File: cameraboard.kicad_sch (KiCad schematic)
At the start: 6 parts, among them J1 Conn_02x05_Odd_Even, Q1 Nikla_Vision, Q2 SSM3J133TU,LF

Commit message: Moved nicla model to kicad_libs, exported pcb model
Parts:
- R1, R2: footprint Resistor_SMD:R_0603_1608Metric_Pad0.98x0.95mm_HandSolder -> (none)
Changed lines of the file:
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@@
       (effects (font (size 0.762 0.762)) (justify left))
     )
-    (property "Footprint" "Resistor_SMD:R_0603_1608Metric_Pad0.98x0.95mm_HandSolder" (id 2) (at 42.672 42.418 0)
+    (property "Footprint" "" (id 2) (at 42.672 42.418 0)
       (effects (font (size 1.27 1.27)) hide)
     )
@@
       (effects (font (size 0.762 0.762)))
     )
-    (property "Footprint" "Resistor_SMD:R_0603_1608Metric_Pad0.98x0.95mm_HandSolder" (id 2) (at 47.625 37.084 0)
+    (property "Footprint" "" (id 2) (at 47.625 37.084 0)
       (effects (font (size 1.27 1.27)) hide)
     )

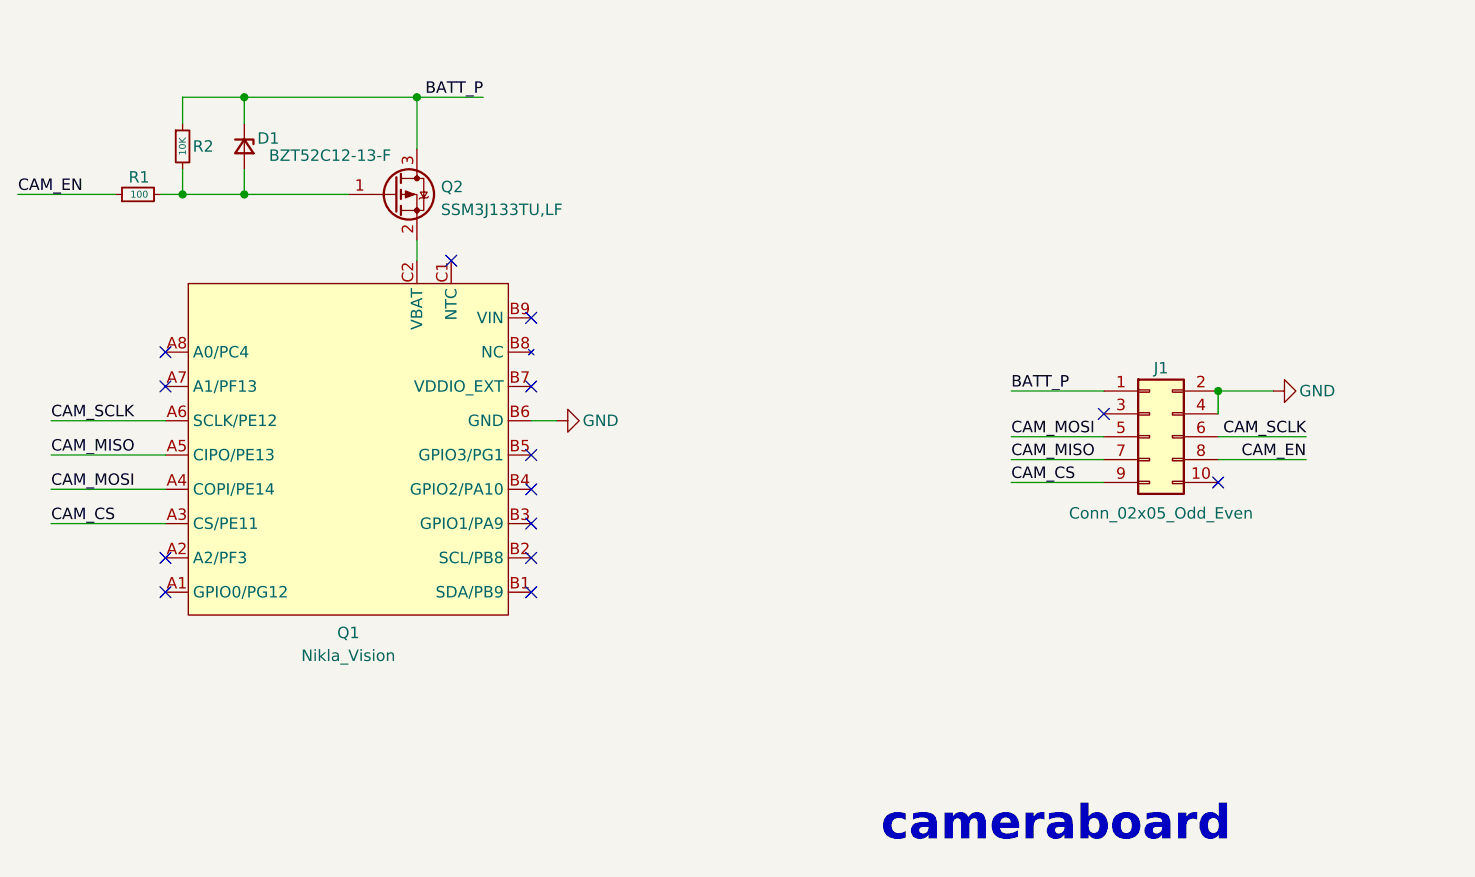
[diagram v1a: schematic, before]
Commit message: Changed board shape and rewired
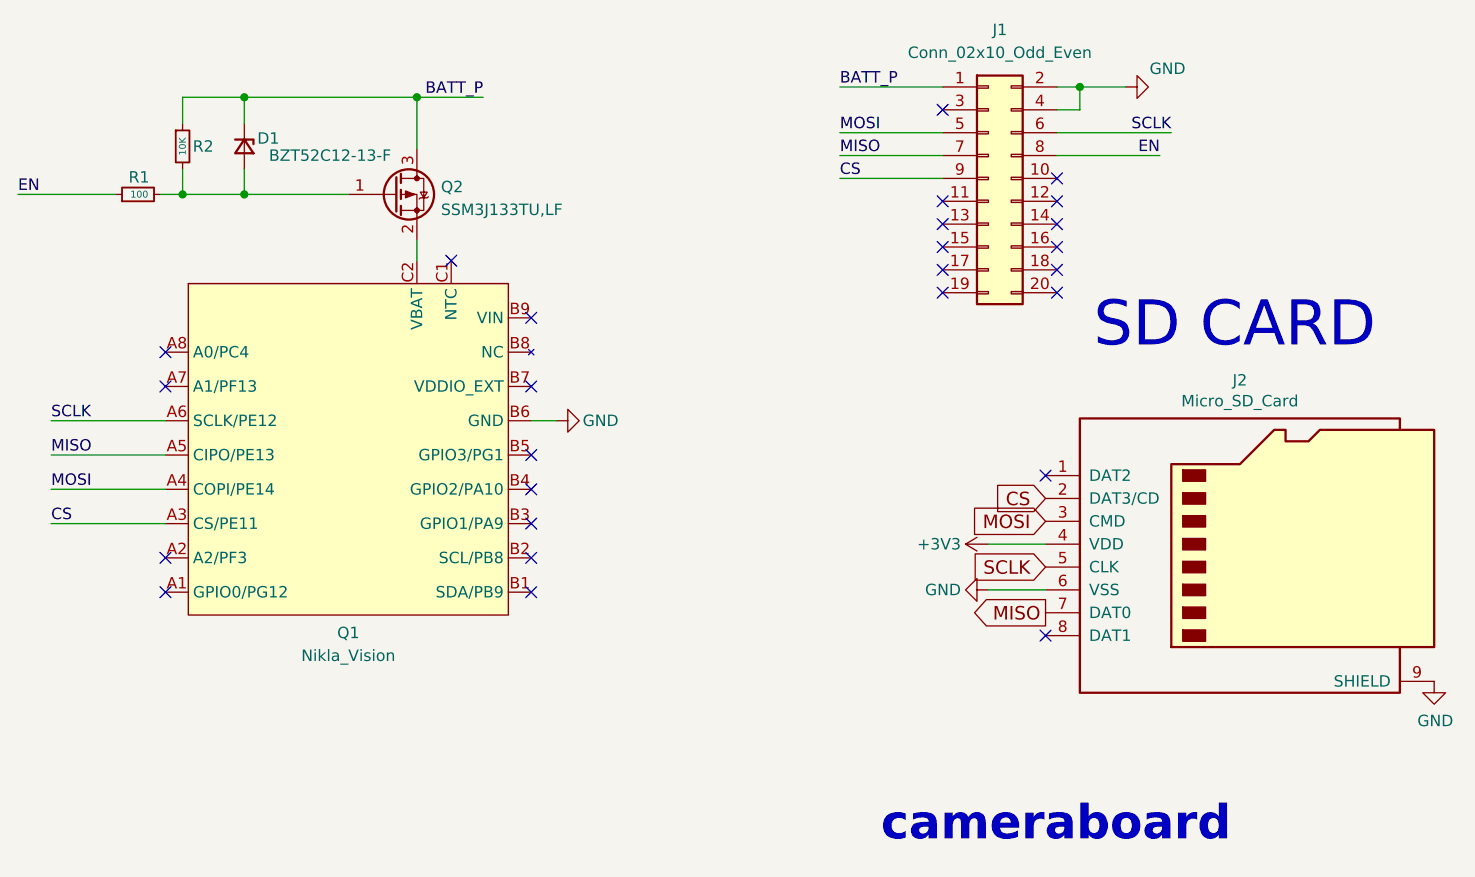
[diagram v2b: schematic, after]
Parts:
- removed J1: Conn_02x05_Odd_Even, Connector_PinSocket_1.27mm:PinSocket_2x05_P1.27mm_Vertical_SMD, symbol Connector_Generic:Conn_02x05_Odd_Even
- added J1: Conn_02x10_Odd_Even, Connector_PinHeader_1.27mm:PinHeader_2x10_P1.27mm_Vertical, symbol Connector_Generic:Conn_02x10_Odd_Even
- added J2: Micro_SD_Card, cameraboard:microSD_HC_Molex_104031-0811, symbol Connector:Micro_SD_Card
- R1, R2: footprint (none) -> Resistor_SMD:R_0603_1608Metric_Pad0.98x0.95mm_HandSolder
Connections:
- net BATT_P: now also J1.1 (Pin_1)
- net GND: now also J1.2 (Pin_2), J1.4 (Pin_4), J2.6 (VSS), J2.9 (SHIELD)
- net CAM_CS renamed CS
- net CS: now also J1.9 (Pin_9), J2.2 (DAT3/CD)
- net CAM_EN renamed EN
- net EN: now also J1.8 (Pin_8)
- net CAM_MISO renamed MISO
- net MISO: now also J1.7 (Pin_7), J2.7 (DAT0)
- net CAM_MOSI renamed MOSI
- net MOSI: now also J1.5 (Pin_5), J2.3 (CMD)
- net CAM_SCLK renamed SCLK
- net SCLK: now also J1.6 (Pin_6), J2.5 (CLK)
- new net +3V3: J2.4 (VDD)
- no-connect marks 14 -> 26
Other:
- note added: "SD CARD"

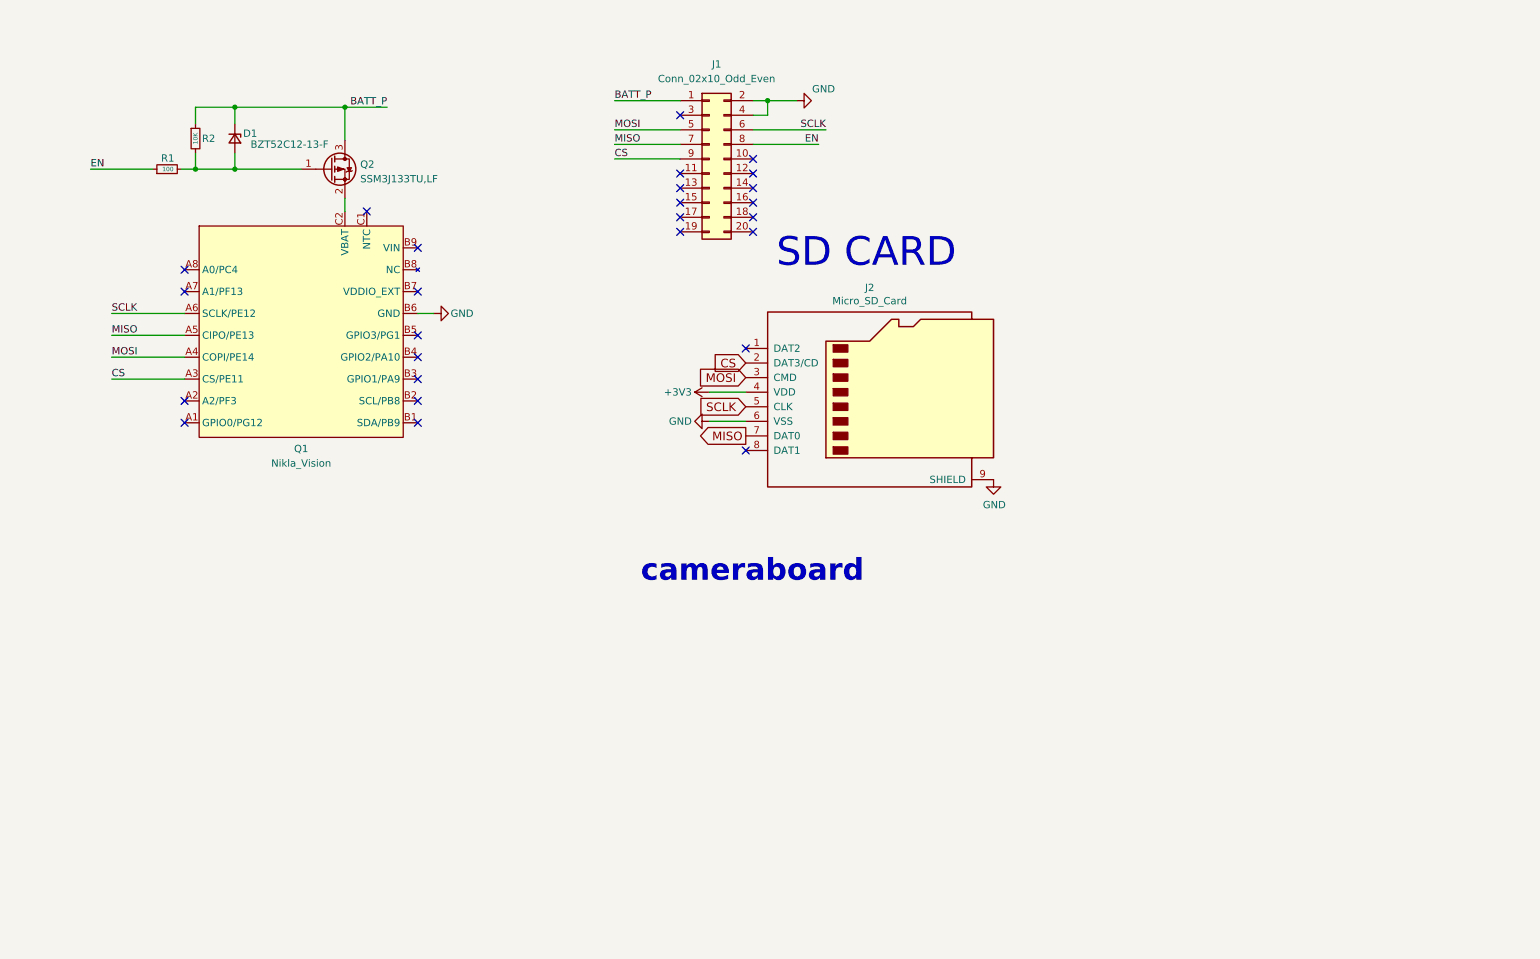
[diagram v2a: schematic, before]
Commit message: Schematic fixes and re-routing
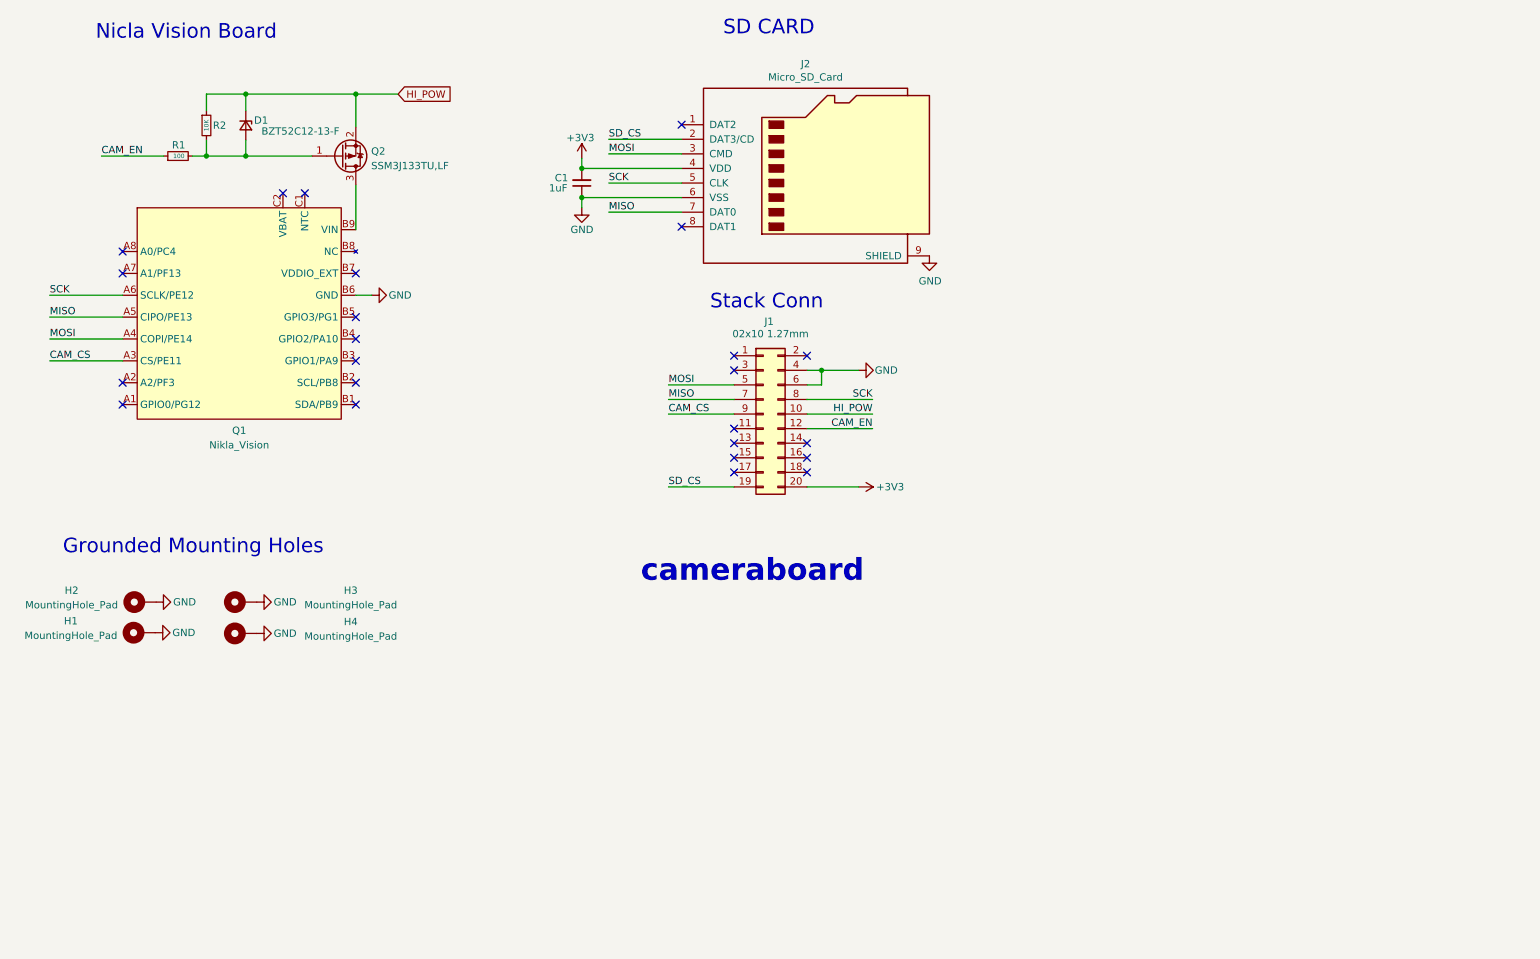
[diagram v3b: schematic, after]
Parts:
- added C1: 1uF, Capacitor_SMD:C_0603_1608Metric_Pad1.08x0.95mm_HandSolder, symbol Device:C_Small
- added H1, H2, H3, H4: MountingHole_Pad, mainboard:MountingHole, symbol Mechanical:MountingHole_Pad
- J1: value Conn_02x10_Odd_Even -> 02x10 1.27mm
- J2: footprint cameraboard:microSD_HC_Molex_104031-0811 -> cameraboard:MOLEX_503398-1892
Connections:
- net +3V3: now also J1.20 (Pin_20), C1.2
- net GND: now also J1.6 (Pin_6), C1.1, H1.1, H2.1, H3.1, H4.1; no longer J1.2 (Pin_2)
- net HI_POW: now reaches J1.10 (Pin_10)
- net HI_POW: now also D1.1 (K), Q2.2 (S), R2.1
- net CAM_EN: now reaches J1.12 (Pin_12)
- net CAM_EN: now also R1.1
- net SD_CS: now reaches J1.19 (Pin_19)
- net SD_CS: now also J2.2 (DAT3/CD)
- net at Q1.B9 (VIN): now also Q2.3 (D)
- net at Q1.C2 (VBAT): no longer Q2.2 (S)
- removed net BATT_P: D1.1 (K), J1.1 (Pin_1), Q2.3 (D), R2.1
- net CS renamed CAM_CS
- net CAM_CS: no longer J2.2 (DAT3/CD)
- net EN renamed SCK
- net SCK: now also J2.5 (CLK), Q1.A6 (SCLK/PE12); no longer R1.1
- removed net SCLK: J1.6 (Pin_6), J2.5 (CLK), Q1.A6 (SCLK/PE12)
- no-connect marks 26 -> 24
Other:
- note added: "Grounded Mounting Holes"
- note added: "Nicla Vision Board"
- note added: "Stack Conn"
- moved on the sheet: D1, J1, J2, Q1, Q2, R1, R2

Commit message: Moved stuff into place
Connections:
- net CAM_EN: now also J1.10 (Pin_10); no longer J1.12 (Pin_12)
- net HI_POW: now also J1.8 (Pin_8); no longer J1.10 (Pin_10)
- net SCK: now also J1.12 (Pin_12); no longer J1.8 (Pin_8)
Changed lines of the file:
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@@
     (effects (font (size 1.27 1.27)) (justify left bottom))
   )
-  (label "CAM_EN" (at 165.608 87.63 180)
+  (label "CAM_EN" (at 165.608 85.09 180)
     (effects (font (size 1.27 1.27)) (justify right bottom))
   )
@@
     (effects (font (size 1.27 1.27)) (justify left bottom))
   )
-  (label "HI_POW" (at 165.608 85.09 180)
+  (label "HI_POW" (at 165.608 82.55 180)
     (effects (font (size 1.27 1.27)) (justify right bottom))
   )
@@
     (effects (font (size 1.27 1.27)) (justify left bottom))
   )
-  (label "SCK" (at 165.608 82.55 180)
+  (label "SCK" (at 165.608 87.63 180)
     (effects (font (size 1.27 1.27)) (justify right bottom))
   )

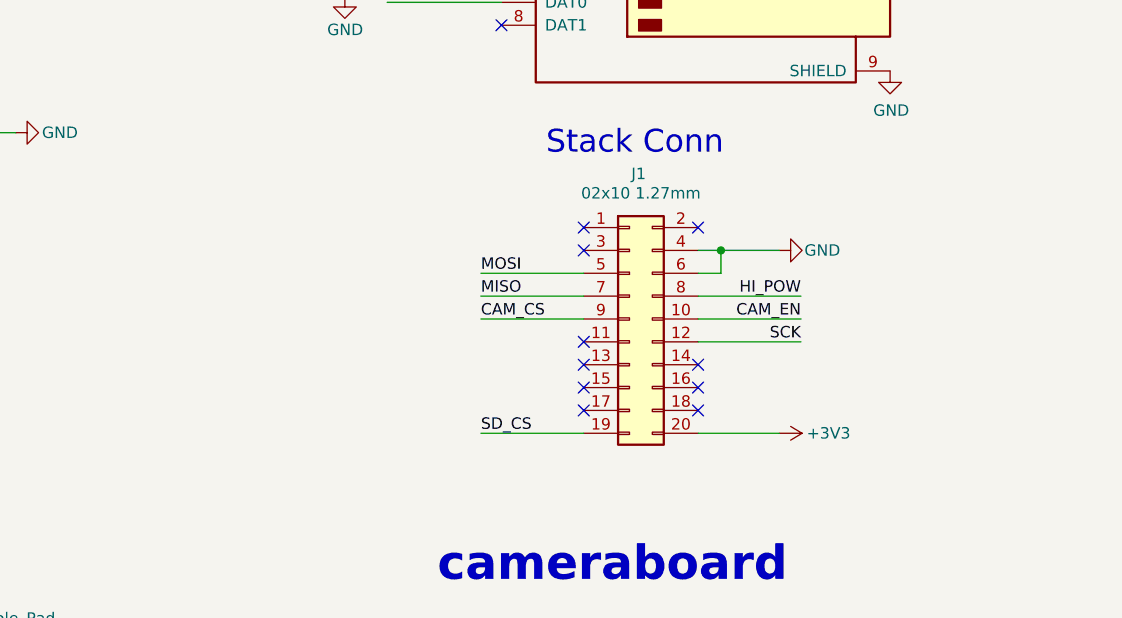
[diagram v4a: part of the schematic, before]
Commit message: stack connectors changes
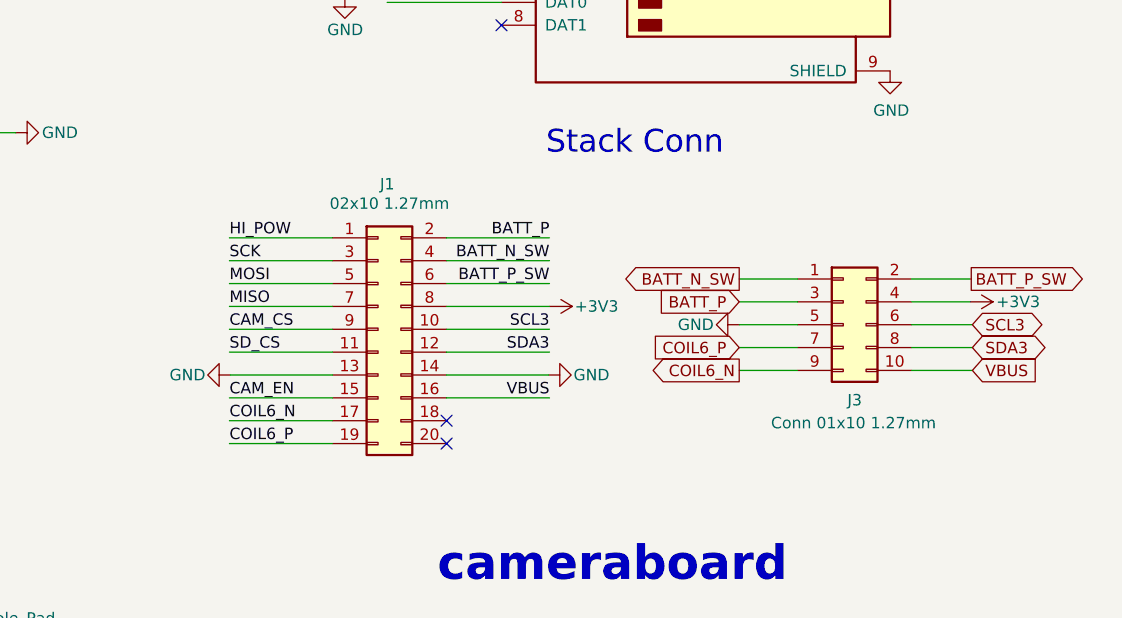
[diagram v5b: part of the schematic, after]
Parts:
- added J3: Conn 01x10 1.27mm, cameraboard:SAMTEC_FLE-105-01-G-DV-A, symbol Connector_Generic:Conn_02x05_Odd_Even
- J1: footprint Connector_PinHeader_1.27mm:PinHeader_2x10_P1.27mm_Vertical -> cameraboard:SAMTEC_TFM-110-12-L-D-A
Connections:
- net +3V3: now also J1.8 (Pin_8), J3.4 (Pin_4); no longer J1.20 (Pin_20)
- net CAM_EN: now also J1.15 (Pin_15); no longer J1.10 (Pin_10)
- net GND: now also J1.13 (Pin_13), J1.14 (Pin_14), J3.5 (Pin_5); no longer J1.4 (Pin_4), J1.6 (Pin_6)
- net HI_POW: now also J1.1 (Pin_1); no longer J1.8 (Pin_8)
- net SCK: now also J1.3 (Pin_3); no longer J1.12 (Pin_12)
- net SD_CS: now also J1.11 (Pin_11); no longer J1.19 (Pin_19)
- net VBUS: now reaches J1.16 (Pin_16)
- net VBUS: now also J3.10 (Pin_10)
- net COIL6_N: now reaches J1.17 (Pin_17)
- net COIL6_N: now also J3.9 (Pin_9)
- net BATT_P: now reaches J1.2 (Pin_2)
- net BATT_P: now also J3.3 (Pin_3)
- new net BATT_N_SW: J1.4 (Pin_4), J3.1 (Pin_1)
- new net BATT_P_SW: J1.6 (Pin_6), J3.2 (Pin_2)
- new net COIL6_P: J1.19 (Pin_19), J3.7 (Pin_7)
- new net SCL3: J1.10 (Pin_10), J3.6 (Pin_6)
- new net SDA3: J1.12 (Pin_12), J3.8 (Pin_8)
- no-connect marks 24 -> 16
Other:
- moved on the sheet: J1

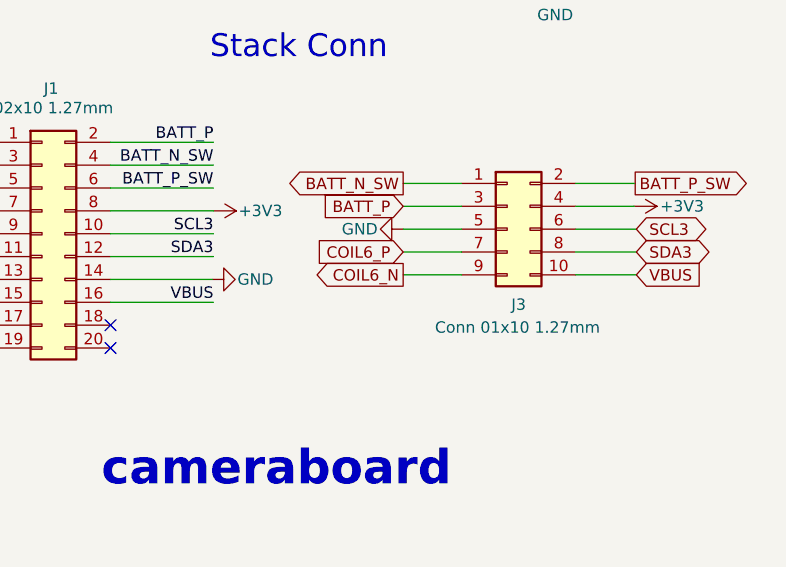
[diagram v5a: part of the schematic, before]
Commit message: Rename VBUS to VUSB and export files
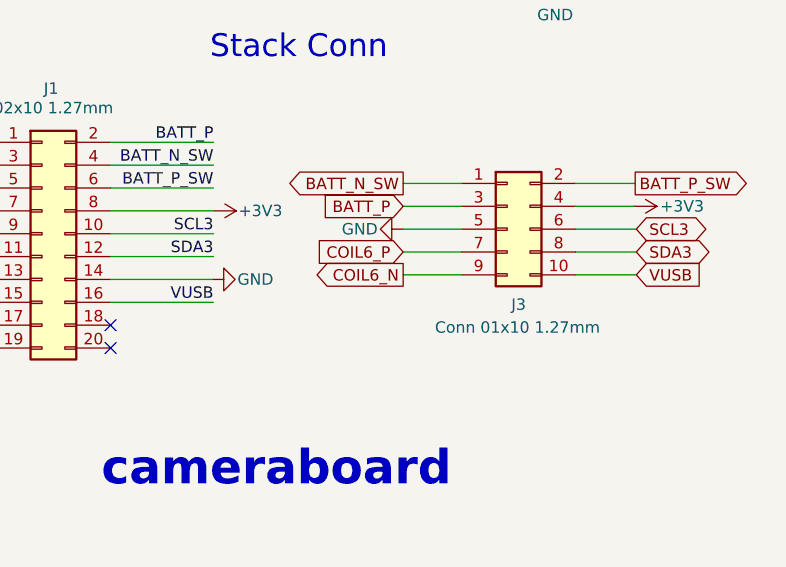
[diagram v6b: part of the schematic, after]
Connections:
- net VBUS renamed VUSB
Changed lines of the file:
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@@
     (effects (font (size 1.27 1.27)) (justify left bottom))
   )
-  (label "VBUS" (at 137.668 93.853 180)
+  (label "VUSB" (at 137.668 93.853 180)
     (effects (font (size 1.27 1.27)) (justify right bottom))
   )
@@
     )
   )
-  (global_label "VBUS" (shape input) (at 184.658 90.805 0) (fields_autoplaced)
+  (global_label "VUSB" (shape input) (at 184.658 90.805 0) (fields_autoplaced)
     (effects (font (size 1.27 1.27)) (justify left))
     (property "Intersheet References" "${INTERSHEET_REFS}" (id 0) (at 191.8808 90.7256 0)
